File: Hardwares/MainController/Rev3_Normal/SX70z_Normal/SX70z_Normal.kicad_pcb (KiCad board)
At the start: 4 copper layers, 95.9 x 72 mm, 50 parts, among them J1 Conn_01x02, J2 Conn_01x03_Socket, J3 Conn_01x02, Q1 Q_NMOS_GSD, Q2 Q_NMOS_GSD, Q5 MMBT3904, Q6 Q_PMOS_GSD, U3 SPX3819M5-L-3-3, U4 ESP32-PICO-D4, U5 OPT4001DTSR

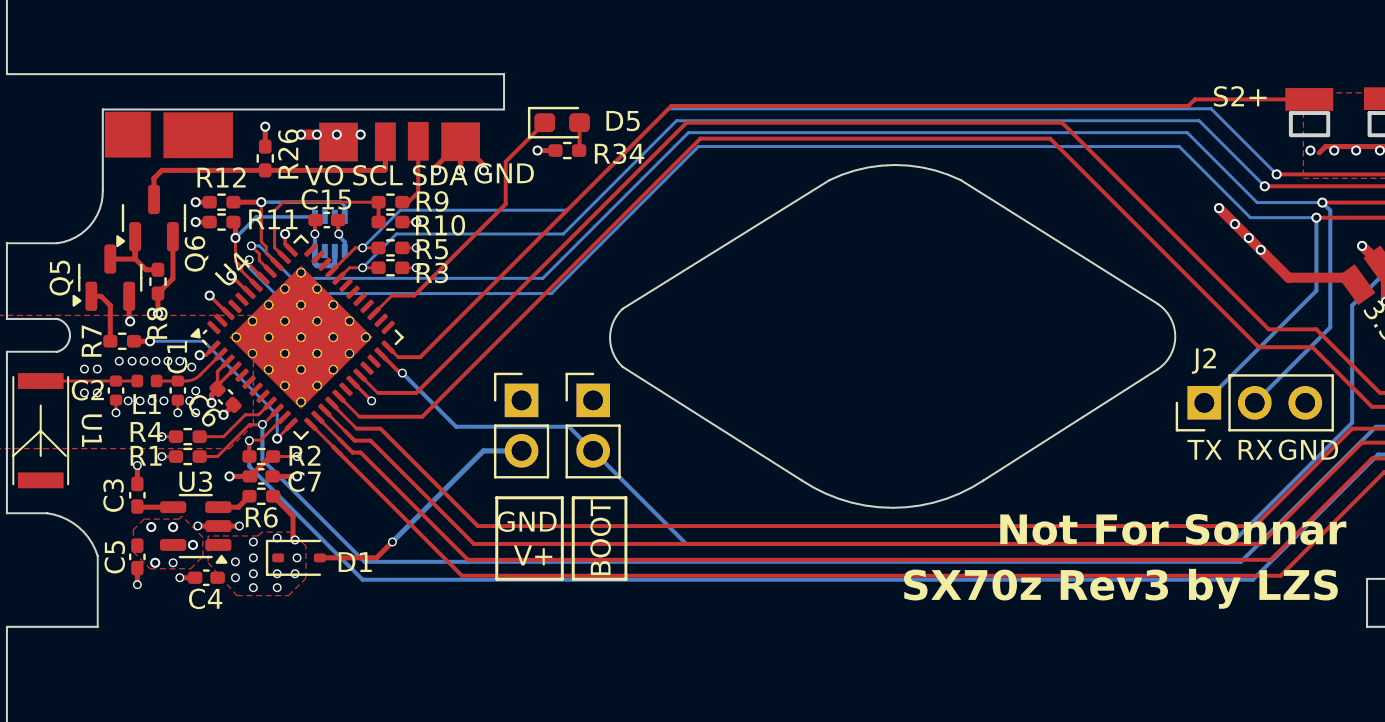
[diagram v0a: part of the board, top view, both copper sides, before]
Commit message: 修改SX70zPCB的小问题，投产机身控制器
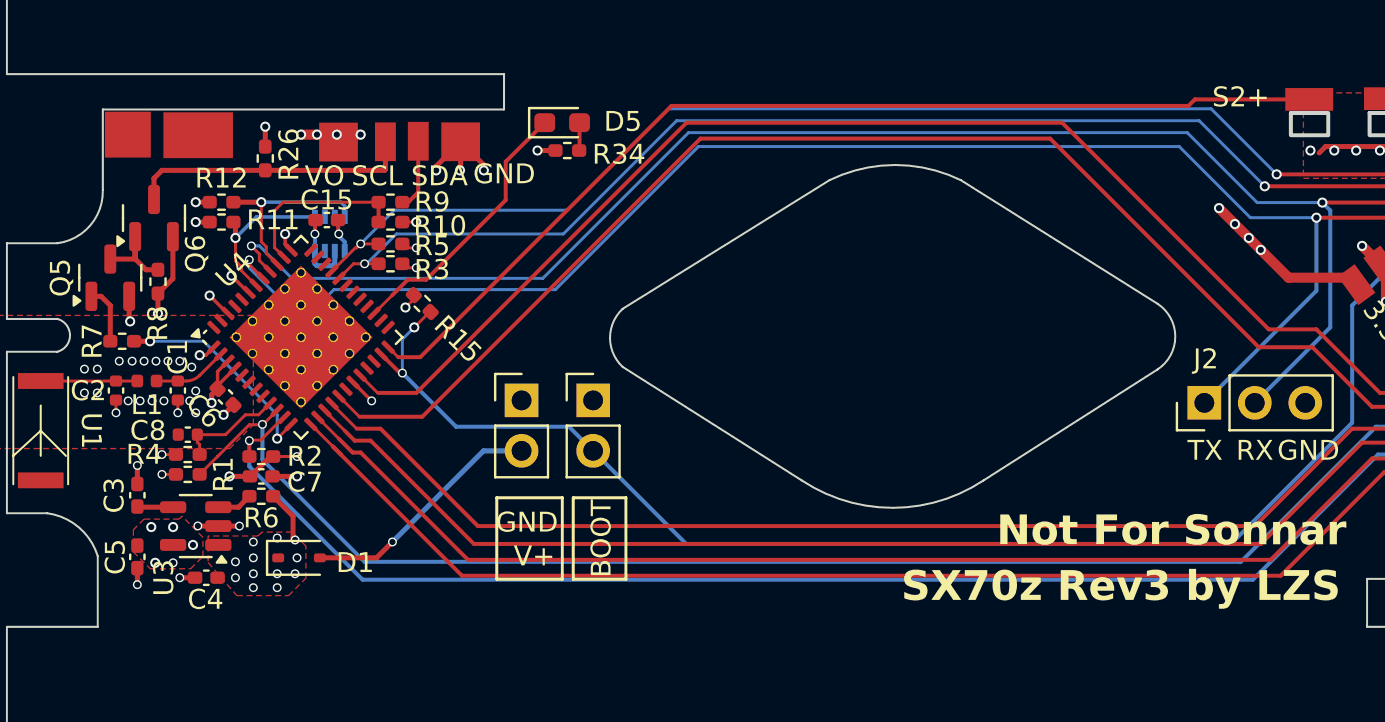
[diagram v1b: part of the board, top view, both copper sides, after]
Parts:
- added C8: 10uf, Capacitor_SMD:C_0402_1005Metric, F.Cu at (34.5, 75.9)
- added R15: 10k, Resistor_SMD:R_0402_1005Metric_Pad0.72x0.64mm_HandSolder, F.Cu at (46.3, 69.3)
- R26: value 2.7k -> 3.3k
- R4: value 330 -> 10k
- moved R1 0.90 mm to (34.5, 77.9)
- moved R4 0.90 mm to (34.5, 76.9)
- moved R3 0.20 mm to (44.7, 67.3)
- moved R5 0.20 mm to (44.7, 66.3)
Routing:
- net /BOOT: track 71.5 -> 75.2 mm, vias 2 -> 3
- net /EN: track 4.24 -> 5.37 mm
- net +3.3V: track 78.8 -> 79.6 mm, vias 25 -> 26
